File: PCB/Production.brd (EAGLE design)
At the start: 102.6 x 40 mm, 40 parts, among them IC1 CY8C4245-LQI-LONG, IC2 OPT3001, J1 2x5p-1.27

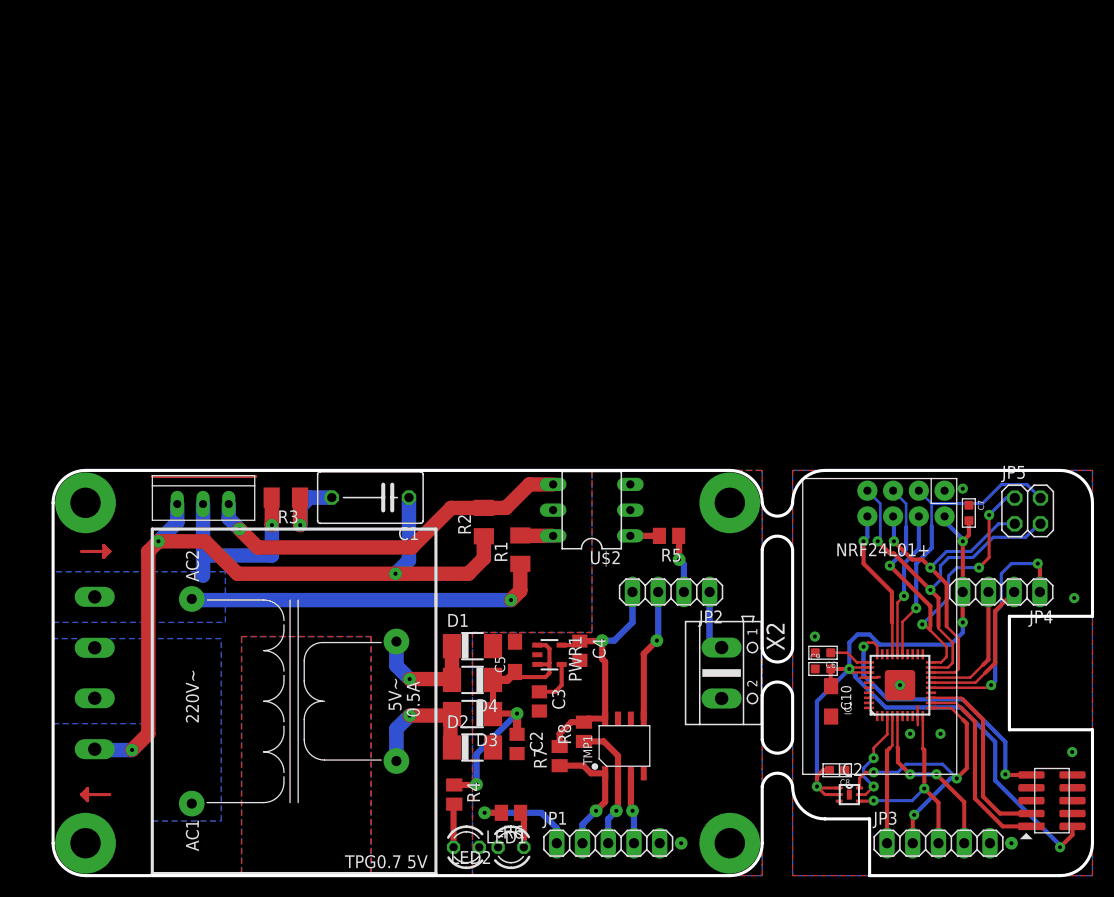
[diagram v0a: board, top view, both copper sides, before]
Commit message: Add new board for Power Controll WiFi Router
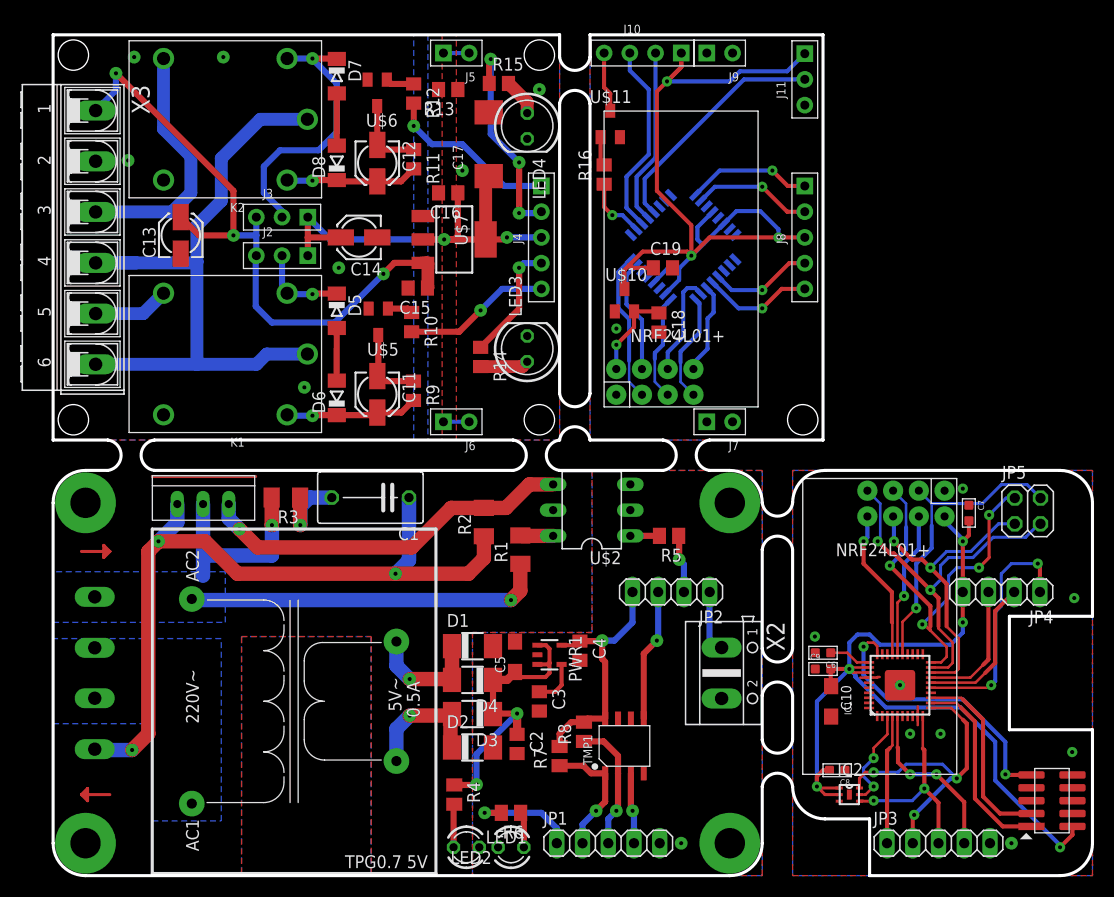
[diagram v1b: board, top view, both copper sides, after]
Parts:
- added C11, C12, C13, C14: (no value), rcl:153CLV-0405
- added C15, C16, C18, C19: (no value), rcl:C0805
- added C17: (no value), rcl:SMC_D
- added D5, D7: (no value), diode:MINIMELF
- added D6, D8: (no value), diode:SOD80C
- added J10: 4p-2.54, Seeed-OPL-Connector:H4-2.54
- added J11, J2, J3: 3p-2.54, Seeed-OPL-Connector:H3-2.54
- added J4, J8: 5p-2.54, Seeed-OPL-Connector:H5-2.54
- added J5, J6, J7, J9: 2p-2.54, Seeed-OPL-Connector:H2-2.54
- added K1, K2: HLS8L-DC5V-S-C, Seeed-OPL-Relay:REY5-19.0X15.0X15.0MM
- added LED3, LED4: (no value), led:LED5MM
- added R10, R11, R12, R13, R14, R15, R16, R9: (no value), rcl:R0805
- added U$10: XC6206_3.3, 74xx:SOT23
- added U$11, U$5, U$6: NSOT23, Mosfet_Logic:SOT23W
- added U$7: ASM1117, 74xx:SOT223
- added U$8: ATMEGAN8, My Atmel:TQFP32-08
- added U$9: NRF24, NRF24l01+:NRF
- added X3: (no value), con-ptr500:AK500/6-H
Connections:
- new net +12V: C13.+, C15.1, J2.3, J3.3, U$7.3, X3.1
- new net +3V3: C18.1, U$10.2, U$9.VCC
- new net +5V2: C14.+, C16.1, C17.+, J2.1, J3.1, J4.3, U$7.2, U$7.4
- new net +5V3: J10.1, J11.1
- new net AGND: C13.-, C14.-, C15.2, C16.2, R13.2, U$5.S, U$6.S, U$7.1, X3.2
- new net CE1: U$8.C1, U$9.CE
- new net CSN1: U$8.C0, U$9.CSN
- new net GND2: C17.-, J5.1, J5.2, J6.1, J6.2, LED3.K, LED4.K, R13.1
- new net GND3: C18.2, C19.2, J11.3, J7.1, J7.2, J9.1, J9.2, U$10.1, U$11.S, U$8.GND, U$8.GND1, U$8.GND2, U$9.GND
- new net IRQ1: U$8.B2, U$9.IRQ
- new net LED1: J4.4, R14.1
- new net LED2: J4.2, R15.1
- new net MISO: U$8.B4, U$9.MISO
- new net MOSI1: U$8.B3, U$9.MOSI
- new net N$27: D5.C, J2.2, K1.2
- new net N$28: C11.+, D6.C, K1.3, R9.2
- new net N$29: D5.A, D6.A
- new net N$30: C11.-, R9.1, U$5.D
- new net N$31: R10.1, U$5.G
- new net N$32: D7.C, J3.2, K2.2
- new net N$33: C12.+, D8.C, K2.3, R11.2
- new net N$34: D7.A, D8.A
- new net N$35: C12.-, R11.1, U$6.D
- new net N$36: R12.1, U$6.G
- new net N$37: K1.4, X3.5
- new net N$38: K1.1, K2.1, X3.4, X3.6
- new net N$39: K2.4, X3.3
- new net N$40: LED3.A, R14.2
- new net N$41: LED4.A, R15.2
- new net N$42: C19.1, J8.3, U$10.3, U$8.AREF, U$8.AVCC, U$8.VCC, U$8.VCC1
- new net N$43: J8.5, U$8.B1
- new net N$44: J8.4, U$8.B0
- new net N$45: J8.1, U$8.D3
- new net N$46: J8.2, U$8.D4
- new net N$47: J10.2, U$8.C5
- new net N$48: J10.3, U$8.C4
- new net N$49: J10.4, U$11.D
- new net N$50: R16.2, U$11.G
- new net N$51: R16.1, U$8.C3
- new net N$52: J11.2, U$8.C6
- new net REL1: J4.5, R10.2
- new net REL2: J4.1, R12.2
- new net SCLK1: U$8.B5, U$9.SCK
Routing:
- net N$42: track 0.00 -> 70.2 mm, vias 0 -> 2
- net N$38: track 0.00 -> 66.9 mm
- net +12V: track 0.00 -> 64.9 mm, vias 0 -> 3
- net +5V2: track 0.00 -> 45.3 mm, vias 0 -> 2
- net N$32: track 0.00 -> 27.6 mm, vias 0 -> 1
- net N$39: track 0.00 -> 24.6 mm
- net N$52: track 0.00 -> 23.5 mm
- net LED2: track 0.00 -> 21.1 mm, vias 0 -> 3
- net N$48: track 0.00 -> 19.2 mm
- net +5V3: track 0.00 -> 18.1 mm, vias 0 -> 1
- net N$47: track 0.00 -> 17.5 mm
- net REL2: track 0.00 -> 17.3 mm, vias 0 -> 1
- net CE1: track 0.00 -> 14.8 mm
- net REL1: track 0.00 -> 14.6 mm, vias 0 -> 1
- net N$28: track 0.00 -> 13.1 mm, vias 0 -> 1
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- added copper zone on layer 1, net AGND
- added copper zone on layer 16, net AGND
- added copper zone on layer 1, net GND2
- added copper zone on layer 16, net GND2
- added copper zone on layer 1, net GND3
- added copper zone on layer 16, net GND3
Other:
- board size 102.6 x 40 mm -> 102.6 x 83 mm
